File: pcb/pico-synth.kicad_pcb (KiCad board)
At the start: 2 copper layers, 56.6 x 74.5 mm, 44 parts, among them J1 JST XH 5P, J2 JST XH 2P, J3 JST XH 4P, J4 JST XH 3P, SW1 Rotary_Encoder_Switch, U1 Pico, U2 6N137, U3 24LC512, U4 TLV272, U5 MCP4822

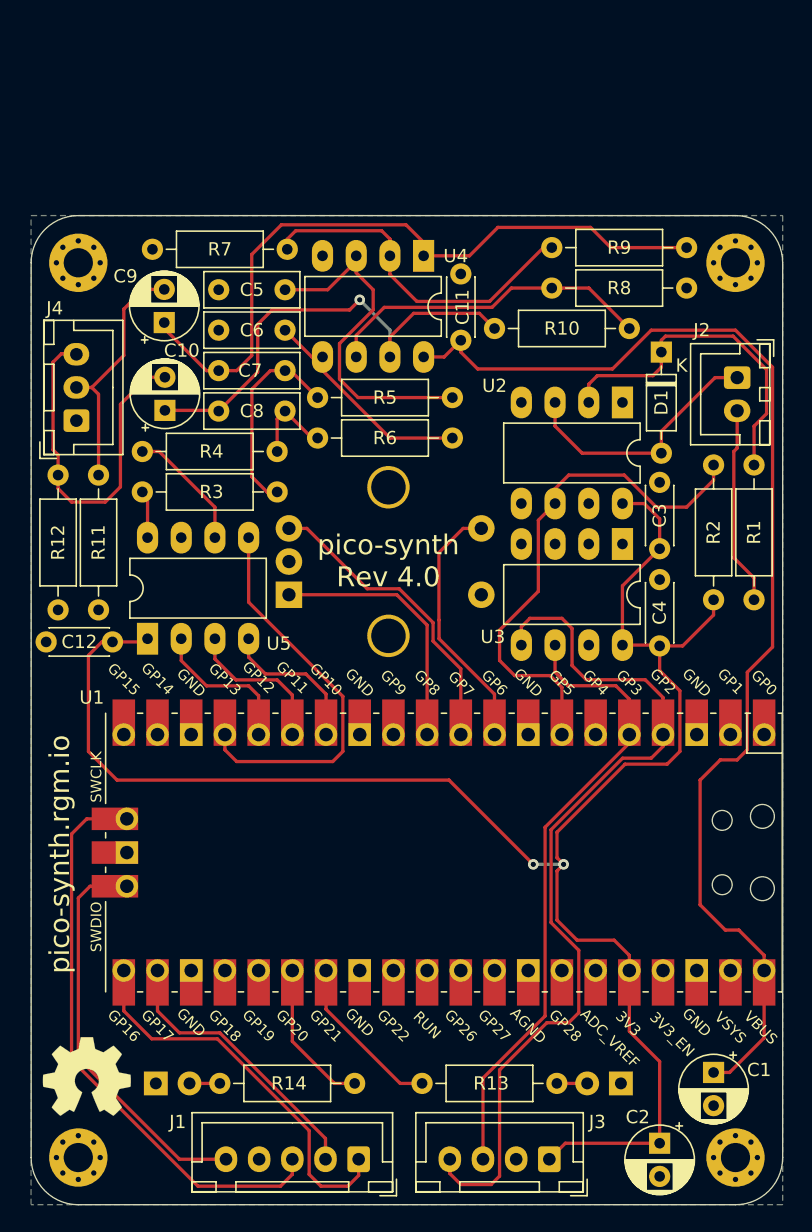
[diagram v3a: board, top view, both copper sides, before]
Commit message: pcb: new hardware revision: 4.2
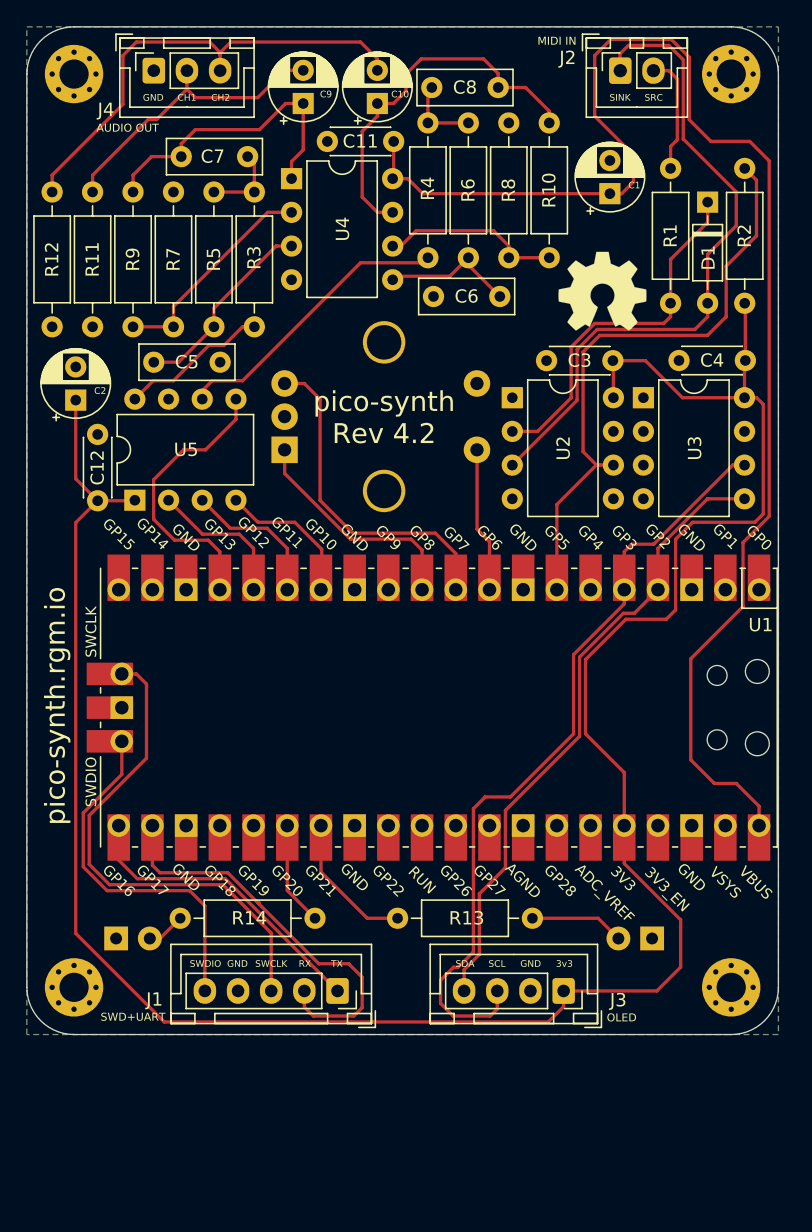
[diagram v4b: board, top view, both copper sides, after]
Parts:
- D2, D3: value LED -> 3mm UB
- H1, H2, H3, H4: value MountingHole -> MountingHole_Pad
- J1: footprint Connector_JST:JST_XH_B5B-XH-A_1x05_P2.50mm_Vertical -> Connector_JST_with_PinSocket:JST_XH_B5B-XH-A_PinSocket_1x05_P2.50mm_Vertical
- J2: footprint Connector_JST:JST_XH_B2B-XH-A_1x02_P2.50mm_Vertical -> Connector_JST_with_PinSocket:JST_XH_B2B-XH-A_PinSocket_1x02_P2.50mm_Vertical
- J3: footprint Connector_JST:JST_XH_B4B-XH-A_1x04_P2.50mm_Vertical -> Connector_JST_with_PinSocket:JST_XH_B4B-XH-A_PinSocket_1x04_P2.50mm_Vertical
- J4: footprint Connector_JST:JST_XH_B3B-XH-A_1x03_P2.50mm_Vertical -> Connector_JST_with_PinSocket:JST_XH_B3B-XH-A_PinSocket_1x03_P2.50mm_Vertical
- U2, U3, U4, U5: footprint Package_DIP:DIP-8_W7.62mm_LongPads -> Package_DIP:DIP-8_W7.62mm
- moved C2 71.2 mm to (120.8, 83.0), turned to 90 degrees
- moved REF** 70.8 mm to (160.5, 74.8)
- moved C1 66.7 mm to (161.1, 67.4), turned to 90 degrees
- moved R9 41.9 mm to (125.2, 67.3), turned to -90 degrees
- moved R1 33.1 mm to (165.7, 65.5), turned to -90 degrees
- moved C10 28.1 mm to (143.6, 60.6)
- moved R4 27.2 mm to (147.4, 62.1), turned to -90 degrees
- moved J4 27.0 mm to (126.7, 58.2), turned to 0 degrees
- moved C8 26.8 mm to (147.7, 59.4), turned to 0 degrees
- moved J2 24.8 mm to (161.9, 58.2), turned to 0 degrees
- moved R3 22.7 mm to (134.3, 67.3), turned to -90 degrees
- moved R2 22.5 mm to (171.3, 75.7)
- moved R11 21.3 mm to (122.1, 67.3)
- moved R12 21.3 mm to (119.1, 67.3)
- moved C9 19.6 mm to (138.0, 60.6)
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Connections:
- H1 pad 1: (no net) -> GND
- H2 pad 1: (no net) -> GND
- H3 pad 1: (no net) -> GND
- H4 pad 1: (no net) -> GND
- SW1 pad S1: ENC_BT -> GND
- SW1 pad S2: GND -> ENC_BT
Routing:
- net +3V3: track 132.4 -> 173.3 mm, vias 2 -> 0
- net Net-(D1-Pad2): track 19.7 -> 50.3 mm
- net Net-(C7-Pad2): track 53.2 -> 22.9 mm
- net SDA: track 67.0 -> 48.0 mm
- net +5V: track 91.6 -> 108.4 mm
- net CH2: track 9.50 -> 21.8 mm
- net Net-(C5-Pad1): track 26.6 -> 14.8 mm
- net SCL: track 47.8 -> 59.1 mm
- net Net-(R10-Pad2): track 24.9 -> 13.6 mm
- net Net-(R7-Pad2): track 26.4 -> 16.4 mm
- net DBG_RX: track 21.3 -> 30.7 mm
- net Net-(C7-Pad1): track 15.4 -> 5.93 mm
- net ENC_BT: track 19.4 -> 10.9 mm
- net LDAC: track 29.8 -> 21.5 mm
- net Net-(C10-Pad2): track 27.7 -> 35.7 mm
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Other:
- board size 56.6 x 74.5 mm -> 56.6 x 75.9 mm
- board text added: "3v3"
- board text added: "CH1"
- board text added: "CH2"
- board text added: "GND"
- board text added: "RX"
- board text added: "SCL"
- board text added: "SDA"
- board text added: "SINK"
- board text added: "SRC"
- board text added: "SWCLK"
- board text added: "SWDIO"
- board text added: "TX"
- board text added: "pico-synth Rev 4.2"
- board text removed: "pico-synth Rev 4.0"
